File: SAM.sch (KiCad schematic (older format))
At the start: 61 parts, among them J301 CONN_02x05, 0.05\", SW301 Switch_DPST, SW302 Switch_DPST, U301 ATSAMD21J18A-MUT, U302 AAT4610, U303 AAT4610, X301 FC-135

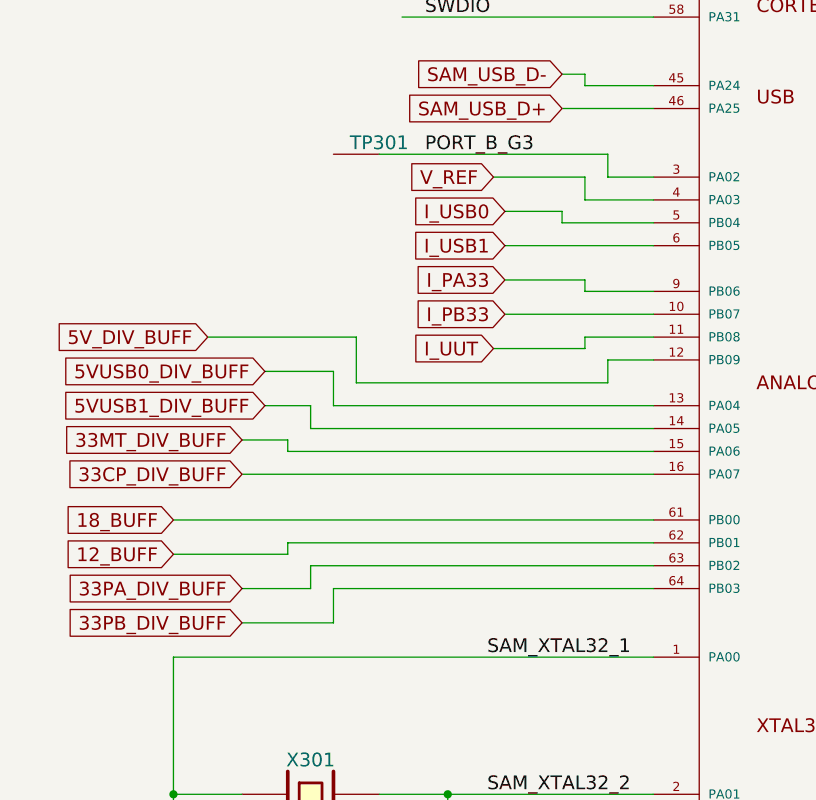
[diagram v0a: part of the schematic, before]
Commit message: significant progress on placement, sch changes for adc routing
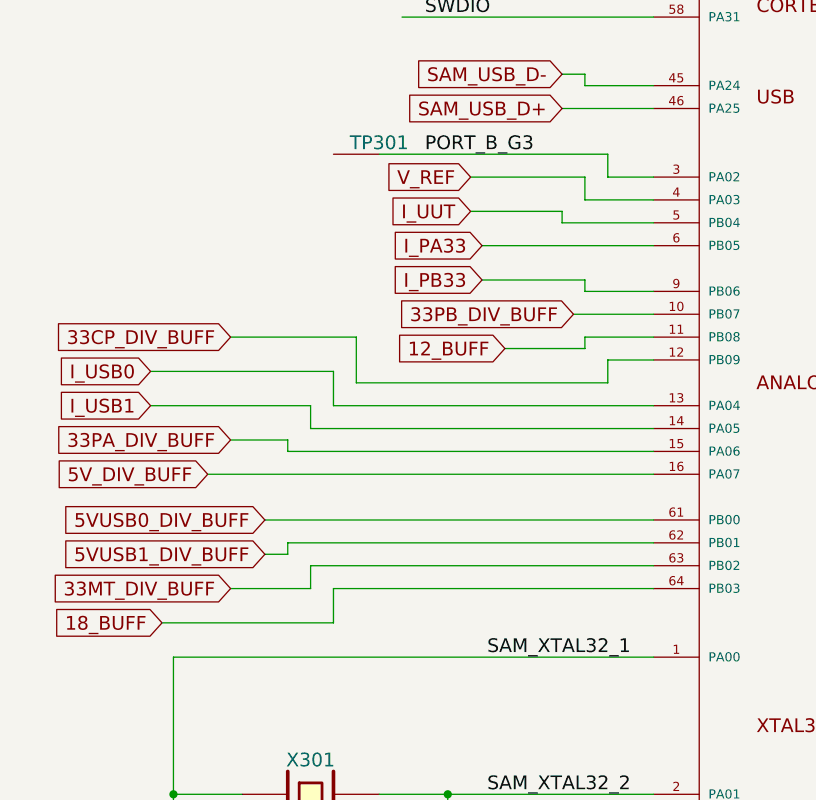
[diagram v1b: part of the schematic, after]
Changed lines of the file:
@@
 $EndComp
 $Comp
-L +3.3V #PWR070
+L +3.3V #PWR069
 U 1 1 553704BB
 P 4600 2250
-F 0 "#PWR070" H 4600 2100 50  0001 C CNN
+F 0 "#PWR069" H 4600 2100 50  0001 C CNN
 F 1 "+3.3V" H 4600 2390 50  0000 C CNN
 F 2 "" H 4600 2250 60  0000 C CNN
@@
 Text GLabel 3500 5550 0    60   Input ~ 0
 SAM_USB_D-
-Text GLabel 3200 6000 0    60   Input ~ 0
+Text GLabel 3100 6000 0    60   Input ~ 0
 V_REF
 Text Label 6800 8000 0    60   ~ 0
@@
 $EndComp
 $Comp
-L GND #PWR071
+L GND #PWR070
 U 1 1 5539EEBD
 P 2500 4000
-F 0 "#PWR071" H 2500 4000 30  0001 C CNN
+F 0 "#PWR070" H 2500 4000 30  0001 C CNN
 F 1 "GND" H 2500 3930 30  0001 C CNN
 F 2 "" H 2500 4000 60  0000 C CNN
@@
 	1    0    0    -1
 $EndComp
-Text GLabel 3250 6150 0    60   Input ~ 0
+Text GLabel 1700 6850 0    60   Input ~ 0
 I_USB0
-Text GLabel 3250 6300 0    60   Input ~ 0
+Text GLabel 1700 7000 0    60   Input ~ 0
 I_USB1
-Text GLabel 3250 6450 0    60   Input ~ 0
+Text GLabel 3150 6300 0    60   Input ~ 0
 I_PA33
-Text GLabel 3250 6600 0    60   Input ~ 0
+Text GLabel 3150 6450 0    60   Input ~ 0
 I_PB33
-Text GLabel 1950 6700 0    60   Input ~ 0
+Text GLabel 1950 7300 0    60   Input ~ 0
 5V_DIV_BUFF
-Text GLabel 2100 7150 0    60   Input ~ 0
+Text GLabel 2050 7800 0    60   Input ~ 0
 33MT_DIV_BUFF
-Text GLabel 2100 7300 0    60   Input ~ 0
+Text GLabel 2050 6700 0    60   Input ~ 0
 33CP_DIV_BUFF
 $Comp
@@
 Text GLabel 7100 5300 2    60   Output ~ 0
 PB33_SHORT
-Text GLabel 2200 6850 0    60   Input ~ 0
+Text GLabel 2200 7500 0    60   Input ~ 0
 5VUSB0_DIV_BUFF
-Text GLabel 2200 7000 0    60   Input ~ 0
+Text GLabel 2200 7650 0    60   Input ~ 0
 5VUSB1_DIV_BUFF
-Text GLabel 2100 7950 0    60   Input ~ 0
+Text GLabel 3550 6600 0    60   Input ~ 0
 33PB_DIV_BUFF
-Text GLabel 2100 7800 0    60   Input ~ 0
+Text GLabel 2050 7150 0    60   Input ~ 0
 33PA_DIV_BUFF
-Text GLabel 1800 7650 0    60   Input ~ 0
+Text GLabel 3250 6750 0    60   Input ~ 0
 12_BUFF
-Text GLabel 1800 7500 0    60   Input ~ 0
+Text GLabel 1750 7950 0    60   Input ~ 0
 18_BUFF
 $Comp
@@
 $EndComp
 $Comp
-L GND #PWR072
+L GND #PWR071
 U 1 1 5542B6FE
 P 13500 6400
-F 0 "#PWR072" H 13500 6400 30  0001 C CNN
+F 0 "#PWR071" H 13500 6400 30  0001 C CNN
 F 1 "GND" H 13500 6330 30  0001 C CNN
 F 2 "" H 13500 6400 60  0000 C CNN
@@
 $EndComp
 $Comp
-L GND #PWR073
+L GND #PWR072
 U 1 1 5542B736
 P 14100 6400
-F 0 "#PWR073" H 14100 6400 30  0001 C CNN
+F 0 "#PWR072" H 14100 6400 30  0001 C CNN
 F 1 "GND" H 14100 6330 30  0001 C CNN
 F 2 "" H 14100 6400 60  0000 C CNN
@@
 $EndComp
 $Comp
-L GND #PWR074
+L GND #PWR073
 U 1 1 5542B978
 P 13400 5100
-F 0 "#PWR074" H 13400 5100 30  0001 C CNN
+F 0 "#PWR073" H 13400 5100 30  0001 C CNN
 F 1 "GND" H 13400 5030 30  0001 C CNN
 F 2 "" H 13400 5100 60  0000 C CNN
@@
 $EndComp
 $Comp
-L GND #PWR075
+L GND #PWR074
 U 1 1 5542B97E
 P 13000 5100
-F 0 "#PWR075" H 13000 5100 30  0001 C CNN
+F 0 "#PWR074" H 13000 5100 30  0001 C CNN
 F 1 "GND" H 13000 5030 30  0001 C CNN
 F 2 "" H 13000 5100 60  0000 C CNN
@@
 $EndComp
 $Comp
-L GND #PWR076
+L GND #PWR075
 U 1 1 5542BC57
 P 15500 5700
-F 0 "#PWR076" H 15500 5700 30  0001 C CNN
+F 0 "#PWR075" H 15500 5700 30  0001 C CNN
 F 1 "GND" H 15500 5630 30  0001 C CNN
 F 2 "" H 15500 5700 60  0000 C CNN
@@
 $EndComp
 $Comp
-L GND #PWR077
+L GND #PWR076
 U 1 1 5542D0CC
 P 13500 8100
-F 0 "#PWR077" H 13500 8100 30  0001 C CNN
+F 0 "#PWR076" H 13500 8100 30  0001 C CNN
 F 1 "GND" H 13500 8030 30  0001 C CNN
 F 2 "" H 13500 8100 60  0000 C CNN
@@
 $EndComp
 $Comp
-L GND #PWR078
+L GND #PWR077
 U 1 1 5542D0D2
 P 14100 8100
-F 0 "#PWR078" H 14100 8100 30  0001 C CNN
+F 0 "#PWR077" H 14100 8100 30  0001 C CNN
 F 1 "GND" H 14100 8030 30  0001 C CNN
 F 2 "" H 14100 8100 60  0000 C CNN
@@
 SWAP: MT9700
 $Comp
-L GND #PWR079
+L GND #PWR078
 U 1 1 5542D0F1
 P 15500 7400
-F 0 "#PWR079" H 15500 7400 30  0001 C CNN
+F 0 "#PWR078" H 15500 7400 30  0001 C CNN
 F 1 "GND" H 15500 7330 30  0001 C CNN
 F 2 "" H 15500 7400 60  0000 C CNN
@@
 	3600 6100 3600 6000
 Wire Wire Line
-	3600 6000 3200 6000
+	3600 6000 3100 6000
 Wire Wire Line
 	2500 4000 2500 3900
@@
 Connection ~ 5400 9200
 Wire Wire Line
-	3900 6300 3250 6300
+	3900 6300 3150 6300
 Wire Wire Line
 	3900 6500 3600 6500
 Wire Wire Line
-	3900 6600 3250 6600
+	3900 6600 3550 6600
 Wire Wire Line
 	2500 7000 3900 7000
@@
 	2300 7200 3900 7200
 Wire Wire Line
-	2100 7300 3900 7300
-Wire Wire Line
-	3900 7500 1800 7500
+	1950 7300 3900 7300
+Wire Wire Line
+	3900 7500 2200 7500
 Wire Wire Line
 	2300 7600 3900 7600
@@
 	3500 6200 3500 6150
 Wire Wire Line
-	3500 6150 3250 6150
+	3500 6150 3100 6150
 Wire Wire Line
 	3600 6500 3600 6450
 Wire Wire Line
-	3600 6450 3250 6450
+	3600 6450 3150 6450
 Wire Wire Line
 	3600 6750 3600 6700
@@
 	2500 7000 2500 6850
 Wire Wire Line
-	2500 6850 2200 6850
-Wire Wire Line
-	2200 7000 2400 7000
+	2500 6850 1700 6850
+Wire Wire Line
+	1700 7000 2400 7000
 Wire Wire Line
 	2400 7000 2400 7100
@@
 	2300 7200 2300 7150
 Wire Wire Line
-	2300 7150 2100 7150
+	2300 7150 2050 7150
 Wire Wire Line
 	2300 7600 2300 7650
 Wire Wire Line
-	2300 7650 1800 7650
+	2300 7650 2200 7650
 Wire Wire Line
 	6800 5000 6800 4850
@@
 	2400 7700 2400 7800
 Wire Wire Line
-	2400 7800 2100 7800
+	2400 7800 2050 7800
 Wire Wire Line
 	2500 7800 2500 7950
 Wire Wire Line
-	2500 7950 2100 7950
+	2500 7950 1750 7950
 Wire Wire Line
 	13800 5400 14200 5400
@@
 	2600 6900 2600 6700
 Wire Wire Line
-	2600 6700 1950 6700
-Text GLabel 3200 6750 0    60   Input ~ 0
+	2600 6700 2050 6700
+Text GLabel 3100 6150 0    60   Input ~ 0
 I_UUT
 Wire Wire Line
-	3200 6750 3600 6750
+	3250 6750 3600 6750
 $Comp
 L TM_C C311
@@
 $EndComp
 $Comp
-L GND #PWR080
+L GND #PWR079
 U 1 1 55447150
 P 11300 3200
-F 0 "#PWR080" H 11300 3200 30  0001 C CNN
+F 0 "#PWR079" H 11300 3200 30  0001 C CNN
 F 1 "GND" H 11300 3130 30  0001 C CNN
 F 2 "" H 11300 3200 60  0000 C CNN
@@
 $EndComp
 $Comp
-L GND #PWR081
+L GND #PWR080
 U 1 1 5544715D
 P 10000 3200
-F 0 "#PWR081" H 10000 3200 30  0001 C CNN
+F 0 "#PWR080" H 10000 3200 30  0001 C CNN
 F 1 "GND" H 10000 3130 30  0001 C CNN
 F 2 "" H 10000 3200 60  0000 C CNN
@@
 $EndComp
 $Comp
-L +3.3V #PWR082
+L +3.3V #PWR081
 U 1 1 55447163
 P 11400 1600
-F 0 "#PWR082" H 11400 1450 50  0001 C CNN
+F 0 "#PWR081" H 11400 1450 50  0001 C CNN
 F 1 "+3.3V" H 11400 1740 50  0000 C CNN
 F 2 "" H 11400 1600 60  0000 C CNN
@@
 $EndComp
 $Comp
-L GND #PWR083
+L GND #PWR082
 U 1 1 55447189
 P 14600 3200
-F 0 "#PWR083" H 14600 3200 30  0001 C CNN
+F 0 "#PWR082" H 14600 3200 30  0001 C CNN
 F 1 "GND" H 14600 3130 30  0001 C CNN
 F 2 "" H 14600 3200 60  0000 C CNN
@@
 $EndComp
 $Comp
-L GND #PWR084
+L GND #PWR083
 U 1 1 55447196
 P 13300 3200
-F 0 "#PWR084" H 13300 3200 30  0001 C CNN
+F 0 "#PWR083" H 13300 3200 30  0001 C CNN
 F 1 "GND" H 13300 3130 30  0001 C CNN
 F 2 "" H 13300 3200 60  0000 C CNN
@@
 $EndComp
 $Comp
-L +3.3V #PWR085
+L +3.3V #PWR084
 U 1 1 5544719C
 P 14700 1600
-F 0 "#PWR085" H 14700 1450 50  0001 C CNN
+F 0 "#PWR084" H 14700 1450 50  0001 C CNN
 F 1 "+3.3V" H 14700 1740 50  0000 C CNN
 F 2 "" H 14700 1600 60  0000 C CNN
@@
 TEST_IN_PROGRESS_LED
 $Comp
-L GND #PWR086
+L GND #PWR085
 U 1 1 55448FCB
 P 11100 8500
-F 0 "#PWR086" H 11100 8250 60  0001 C CNN
+F 0 "#PWR085" H 11100 8250 60  0001 C CNN
 F 1 "GND" H 11100 8350 60  0000 C CNN
 F 2 "" H 11100 8500 60  0000 C CNN
@@
 $EndComp
 $Comp
-L GND #PWR087
+L GND #PWR086
 U 1 1 55448FF0
 P 10600 8500
-F 0 "#PWR087" H 10600 8250 60  0001 C CNN
+F 0 "#PWR086" H 10600 8250 60  0001 C CNN
 F 1 "GND" H 10600 8350 60  0000 C CNN
 F 2 "" H 10600 8500 60  0000 C CNN
@@
 	10600 8500 10600 8400
 $Comp
-L GND #PWR088
+L GND #PWR087
 U 1 1 55449007
 P 9600 8500
-F 0 "#PWR088" H 9600 8250 60  0001 C CNN
+F 0 "#PWR087" H 9600 8250 60  0001 C CNN
 F 1 "GND" H 9600 8350 60  0000 C CNN
 F 2 "" H 9600 8500 60  0000 C CNN
@@
 	9600 8500 9600 8400
 $Comp
-L GND #PWR089
+L GND #PWR088
 U 1 1 5544901E
 P 10100 8500
-F 0 "#PWR089" H 10100 8250 60  0001 C CNN
+F 0 "#PWR088" H 10100 8250 60  0001 C CNN
 F 1 "GND" H 10100 8350 60  0000 C CNN
 F 2 "" H 10100 8500 60  0000 C CNN
@@
 Connection ~ 8700 4000
 $Comp
-L GND #PWR090
+L GND #PWR089
 U 1 1 554885D5
 P 8700 4600
-F 0 "#PWR090" H 8700 4350 60  0001 C CNN
+F 0 "#PWR089" H 8700 4350 60  0001 C CNN
 F 1 "GND" H 8700 4450 60  0000 C CNN
 F 2 "" H 8700 4600 60  0000 C CNN

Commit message: more analog pinswaps
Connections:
- wire segments 204 -> 240
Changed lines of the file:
@@
 Text GLabel 3500 5550 0    60   Input ~ 0
 SAM_USB_D-
-Text GLabel 3100 6000 0    60   Input ~ 0
+Text GLabel 2850 6000 0    60   Input ~ 0
 V_REF
 Text Label 6800 8000 0    60   ~ 0
@@
 	1    0    0    -1
 $EndComp
-Text GLabel 1700 6850 0    60   Input ~ 0
+Text GLabel 2900 6600 0    60   Input ~ 0
 I_USB0
-Text GLabel 1700 7000 0    60   Input ~ 0
+Text GLabel 1550 7800 0    60   Input ~ 0
 I_USB1
+Text GLabel 1550 6700 0    60   Input ~ 0
+I_PA33
+Text GLabel 1550 7300 0    60   Input ~ 0
+I_PB33
 Text GLabel 3150 6300 0    60   Input ~ 0
-I_PA33
-Text GLabel 3150 6450 0    60   Input ~ 0
-I_PB33
-Text GLabel 1950 7300 0    60   Input ~ 0
 5V_DIV_BUFF
-Text GLabel 2050 7800 0    60   Input ~ 0
+Text GLabel 1950 7650 0    60   Input ~ 0
 33MT_DIV_BUFF
-Text GLabel 2050 6700 0    60   Input ~ 0
+Text GLabel 1950 6850 0    60   Input ~ 0
 33CP_DIV_BUFF
 $Comp
@@
 Text GLabel 7100 5300 2    60   Output ~ 0
 PB33_SHORT
-Text GLabel 2200 7500 0    60   Input ~ 0
+Text GLabel 2050 7950 0    60   Input ~ 0
 5VUSB0_DIV_BUFF
-Text GLabel 2200 7650 0    60   Input ~ 0
+Text GLabel 3400 6150 0    60   Input ~ 0
 5VUSB1_DIV_BUFF
-Text GLabel 3550 6600 0    60   Input ~ 0
+Text GLabel 1950 7000 0    60   Input ~ 0
 33PB_DIV_BUFF
-Text GLabel 2050 7150 0    60   Input ~ 0
+Text GLabel 3300 6450 0    60   Input ~ 0
 33PA_DIV_BUFF
-Text GLabel 3250 6750 0    60   Input ~ 0
+Text GLabel 3000 6750 0    60   Input ~ 0
 12_BUFF
-Text GLabel 1750 7950 0    60   Input ~ 0
+Text GLabel 1650 7500 0    60   Input ~ 0
 18_BUFF
 $Comp
@@
 Connection ~ 4900 2400
 Wire Wire Line
-	4900 2400 4900 4600
+	4900 2400 4900 3200
+Wire Wire Line
+	4900 3200 4900 4600
 Connection ~ 5300 3000
 Connection ~ 5300 2400
@@
 Connection ~ 5400 2400
 Wire Wire Line
-	5400 2400 5400 4600
+	5400 2400 5400 2900
+Wire Wire Line
+	5400 2900 5400 4600
 Wire Wire Line
 	4600 2400 4600 2250
@@
 	5300 3000 3300 3000
 Wire Wire Line
-	5300 2400 5300 4600
+	5300 2400 5300 3000
+Wire Wire Line
+	5300 3000 5300 4600
 Wire Wire Line
 	5100 3100 5100 4600
@@
 	4100 3200 4100 3300
 Wire Wire Line
-	4100 3200 4900 3200
+	4100 3200 4500 3200
+Wire Wire Line
+	4500 3200 4900 3200
 Connection ~ 5700 3200
 Connection ~ 6100 3200
 Wire Wire Line
-	6500 3050 6500 3300
+	6500 3050 6500 3200
+Wire Wire Line
+	6500 3200 6500 3300
 Wire Wire Line
 	6100 3200 6100 3300
 Wire Wire Line
-	5700 3200 6500 3200
-Wire Wire Line
-	5700 3100 5700 4600
+	5700 3200 6100 3200
+Wire Wire Line
+	6100 3200 6500 3200
+Wire Wire Line
+	5700 3100 5700 3200
+Wire Wire Line
+	5700 3200 5700 4600
 Wire Wire Line
 	1800 9400 1800 9450
@@
 	1800 8700 2100 8700
 Wire Wire Line
-	1800 8100 1800 8800
+	1800 8100 1800 8700
+Wire Wire Line
+	1800 8700 1800 8800
 Wire Wire Line
 	6700 7500 8000 7500
@@
 	6700 5500 8000 5500
 Wire Wire Line
-	2700 8700 3900 8700
+	2700 8700 3000 8700
+Wire Wire Line
+	3000 8700 3900 8700
 Wire Wire Line
 	1800 8100 3900 8100
@@
 	3900 5200 2800 5200
 Wire Wire Line
-	4600 2400 5700 2400
+	4600 2400 4900 2400
+Wire Wire Line
+	4900 2400 5300 2400
+Wire Wire Line
+	5300 2400 5400 2400
+Wire Wire Line
+	5400 2400 5500 2400
+Wire Wire Line
+	5500 2400 5700 2400
 Wire Wire Line
 	4500 3300 4500 3200
 Connection ~ 4500 3200
 Wire Wire Line
-	4900 9100 4900 9400
-Wire Wire Line
-	4900 9200 5600 9200
+	4900 9100 4900 9200
+Wire Wire Line
+	4900 9200 4900 9400
+Wire Wire Line
+	4900 9200 5100 9200
+Wire Wire Line
+	5100 9200 5200 9200
+Wire Wire Line
+	5200 9200 5300 9200
+Wire Wire Line
+	5300 9200 5400 9200
+Wire Wire Line
+	5400 9200 5600 9200
 Wire Wire Line
 	5100 9200 5100 9100
@@
 	7800 3100 7600 3100
 Wire Wire Line
-	7600 3000 7600 3500
+	7600 3000 7600 3100
+Wire Wire Line
+	7600 3100 7600 3500
 Wire Wire Line
 	7800 3000 7600 3000
@@
 	3600 6100 3600 6000
 Wire Wire Line
-	3600 6000 3100 6000
+	3600 6000 2850 6000
 Wire Wire Line
 	2500 4000 2500 3900
@@
 	2500 2800 5500 2800
 Wire Wire Line
-	5500 2400 5500 4600
+	5500 2400 5500 2800
+Wire Wire Line
+	5500 2800 5500 4600
 Connection ~ 5500 2400
 Connection ~ 5500 2800
@@
 	3900 6500 3600 6500
 Wire Wire Line
-	3900 6600 3550 6600
-Wire Wire Line
-	2500 7000 3900 7000
-Wire Wire Line
-	2400 7100 3900 7100
-Wire Wire Line
-	2300 7200 3900 7200
-Wire Wire Line
-	1950 7300 3900 7300
-Wire Wire Line
-	3900 7500 2200 7500
-Wire Wire Line
-	2300 7600 3900 7600
-Wire Wire Line
-	2400 7700 3900 7700
-Wire Wire Line
-	2500 7800 3900 7800
+	3900 6600 2900 6600
+Wire Wire Line
+	2300 7000 3900 7000
+Wire Wire Line
+	2200 7100 3900 7100
+Wire Wire Line
+	2100 7200 3900 7200
+Wire Wire Line
+	1550 7300 3900 7300
+Wire Wire Line
+	3900 7500 1650 7500
+Wire Wire Line
+	2150 7600 3900 7600
+Wire Wire Line
+	2250 7700 3900 7700
+Wire Wire Line
+	2350 7800 3900 7800
 Wire Wire Line
 	8000 5700 6700 5700
@@
 	3500 6200 3500 6150
 Wire Wire Line
-	3500 6150 3100 6150
+	3500 6150 3400 6150
 Wire Wire Line
 	3600 6500 3600 6450
 Wire Wire Line
-	3600 6450 3150 6450
+	3600 6450 3300 6450
 Wire Wire Line
 	3600 6750 3600 6700
@@
 	3700 6800 3700 6900
 Wire Wire Line
-	3700 6900 2600 6900
-Wire Wire Line
-	2500 7000 2500 6850
-Wire Wire Line
-	2500 6850 1700 6850
-Wire Wire Line
-	1700 7000 2400 7000
-Wire Wire Line
-	2400 7000 2400 7100
-Wire Wire Line
-	2300 7200 2300 7150
-Wire Wire Line
-	2300 7150 2050 7150
-Wire Wire Line
-	2300 7600 2300 7650
-Wire Wire Line
-	2300 7650 2200 7650
+	3700 6900 2400 6900
+Wire Wire Line
+	2300 7000 2300 6850
+Wire Wire Line
+	2300 6850 1950 6850
+Wire Wire Line
+	1950 7000 2200 7000
+Wire Wire Line
+	2200 7000 2200 7100
+Wire Wire Line
+	2100 7200 2100 7150
+Wire Wire Line
+	2100 7150 1500 7150
+Wire Wire Line
+	2150 7600 2150 7650
+Wire Wire Line
+	2150 7650 1950 7650
 Wire Wire Line
 	6800 5000 6800 4850
@@
 	7000 5150 7100 5150
 Wire Wire Line
-	2400 7700 2400 7800
-Wire Wire Line
-	2400 7800 2050 7800
-Wire Wire Line
-	2500 7800 2500 7950
-Wire Wire Line
-	2500 7950 1750 7950
+	2250 7700 2250 7800
+Wire Wire Line
+	2250 7800 1550 7800
+Wire Wire Line
+	2350 7800 2350 7950
+Wire Wire Line
+	2350 7950 2050 7950
 Wire Wire Line
 	13800 5400 14200 5400
 Wire Wire Line
-	13800 4300 13800 7100
-Wire Wire Line
-	12500 5500 14200 5500
+	13800 4300 13800 5400
+Wire Wire Line
+	13800 5400 13800 7100
+Wire Wire Line
+	12500 5500 13500 5500
+Wire Wire Line
+	13500 5500 14200 5500
 Wire Wire Line
 	13500 5700 13500 5500
@@
 	13000 4300 13000 4400
 Wire Wire Line
-	12800 4300 13800 4300
+	12800 4300 13000 4300
+Wire Wire Line
+	13000 4300 13400 4300
+Wire Wire Line
+	13400 4300 13800 4300
 Connection ~ 13400 4300
 Connection ~ 13000 4300
@@
 	13800 7100 14200 7100
 Wire Wire Line
-	12500 7200 14200 7200
+	12500 7200 13500 7200
+Wire Wire Line
+	13500 7200 14200 7200
 Wire Wire Line
 	13500 7400 13500 7200
@@
 $EndComp
 Wire Wire Line
-	2600 6900 2600 6700
-Wire Wire Line
-	2600 6700 2050 6700
-Text GLabel 3100 6150 0    60   Input ~ 0
+	2400 6900 2400 6700
+Wire Wire Line
+	2400 6700 1550 6700
+Text GLabel 1500 7150 0    60   Input ~ 0
 I_UUT
 Wire Wire Line
-	3250 6750 3600 6750
+	3000 6750 3600 6750
 $Comp
 L TM_C C311
@@
 	11400 1600 11400 1700
 Wire Wire Line
-	10700 2400 12600 2400
+	10700 2400 11000 2400
+Wire Wire Line
+	11000 2400 11300 2400
+Wire Wire Line
+	11300 2400 11400 2400
+Wire Wire Line
+	11400 2400 12600 2400
 Wire Wire Line
 	11400 2400 11400 2300
@@
 	10100 2800 10000 2800
 Wire Wire Line
-	10000 2400 10000 3200
+	10000 2400 10000 2800
+Wire Wire Line
+	10000 2800 10000 3200
 $Comp
 L Switch_DPST SW301
@@
 	14700 1600 14700 1700
 Wire Wire Line
-	14000 2400 15600 2400
+	14000 2400 14300 2400
+Wire Wire Line
+	14300 2400 14600 2400
+Wire Wire Line
+	14600 2400 14700 2400
+Wire Wire Line
+	14700 2400 15600 2400
 Wire Wire Line
 	14700 2400 14700 2300
@@
 	13400 2800 13300 2800
 Wire Wire Line
-	13300 2400 13300 3200
+	13300 2400 13300 2800
+Wire Wire Line
+	13300 2800 13300 3200
 $Comp
 L Switch_DPST SW302
@@
 	8900 3800 8700 3800
 Wire Wire Line
-	8700 3800 8700 4600
+	8700 3800 8700 4000
+Wire Wire Line
+	8700 4000 8700 4200
+Wire Wire Line
+	8700 4200 8700 4400
+Wire Wire Line
+	8700 4400 8700 4600
 Wire Wire Line
 	8900 4400 8700 4400
